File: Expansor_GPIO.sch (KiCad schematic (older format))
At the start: 6 parts

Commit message: version preliminar de la etapa de alimentacion
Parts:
- gave numbers to parts that had none: 6
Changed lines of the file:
@@
 LIBS:Sensores
 LIBS:Reles
+LIBS:Reguladores
+LIBS:Transistores
 LIBS:Wifi_PB-cache
 EELAYER 26 0
@@
 $Descr A4 11693 8268
 encoding utf-8
-Sheet 5 11
+Sheet 5 15
 Title ""
 Date "2017-01-15"
@@
 $EndDescr
 $Comp
-L MCP23017 U?
+L MCP23017 U6
 U 1 1 587AB386
 P 3300 2800
-F 0 "U?" H 3650 1800 50  0000 C CNN
+F 0 "U6" H 3650 1800 50  0000 C CNN
 F 1 "MCP23017" H 3350 2800 50  0000 C CNN
 F 2 "" H 3350 1850 50  0001 L CNN
@@
 $EndComp
 $Comp
-L CP1 C?
+L CP1 C14
 U 1 1 587AB690
 P 2450 1400
-F 0 "C?" H 2565 1446 50  0000 L CNN
+F 0 "C14" H 2565 1446 50  0000 L CNN
 F 1 "CP1" H 2565 1355 50  0000 L CNN
-F 2 "" H 2450 1400 50  0000 C CNN
+F 2 "" H 2450 1400 50  0001 C CNN
 F 3 "" H 2450 1400 50  0000 C CNN
 	1    2450 1400
@@
 $EndComp
 $Comp
-L C C?
+L C C16
 U 1 1 587AB6AE
 P 2900 1400
-F 0 "C?" H 3015 1446 50  0000 L CNN
+F 0 "C16" H 3015 1446 50  0000 L CNN
 F 1 "C" H 3015 1355 50  0000 L CNN
-F 2 "" H 2938 1250 50  0000 C CNN
+F 2 "" H 2938 1250 50  0001 C CNN
 F 3 "" H 2900 1400 50  0000 C CNN
 	1    2900 1400
@@
 $EndComp
 $Comp
-L GND #PWR044
+L GND #PWR39
 U 1 1 587AB8C8
 P 3300 3900
-F 0 "#PWR044" H 3300 3650 50  0001 C CNN
+F 0 "#PWR39" H 3300 3650 50  0001 C CNN
 F 1 "GND" H 3305 3727 50  0000 C CNN
 F 2 "" H 3300 3900 50  0000 C CNN
@@
 	3300 3900 3300 3800
 $Comp
-L GND #PWR045
+L GND #PWR35
 U 1 1 587AB8EE
 P 2700 3900
-F 0 "#PWR045" H 2700 3650 50  0001 C CNN
+F 0 "#PWR35" H 2700 3650 50  0001 C CNN
 F 1 "GND" H 2705 3727 50  0000 C CNN
 F 2 "" H 2700 3900 50  0000 C CNN
@@
 	2450 1050 2450 1250
 $Comp
-L GND #PWR046
+L GND #PWR32
 U 1 1 587ABE16
 P 2450 1600
-F 0 "#PWR046" H 2450 1350 50  0001 C CNN
+F 0 "#PWR32" H 2450 1350 50  0001 C CNN
 F 1 "GND" H 2455 1427 50  0000 C CNN
 F 2 "" H 2450 1600 50  0000 C CNN
@@
 Connection ~ 2900 1200
 $Comp
-L GND #PWR047
+L GND #PWR37
 U 1 1 587ABE80
 P 2900 1600
-F 0 "#PWR047" H 2900 1350 50  0001 C CNN
+F 0 "#PWR37" H 2900 1350 50  0001 C CNN
 F 1 "GND" H 2905 1427 50  0000 C CNN
 F 2 "" H 2900 1600 50  0000 C CNN
@@
 $EndComp
 $Comp
-L +5V #PWR048
+L +5V #PWR31
 U 1 1 587ABF96
 P 2450 1050
-F 0 "#PWR048" H 2450 900 50  0001 C CNN
+F 0 "#PWR31" H 2450 900 50  0001 C CNN
 F 1 "+5V" H 2465 1223 50  0000 C CNN
 F 2 "" H 2450 1050 50  0000 C CNN
@@
 	2350 3200 2800 3200
 $Comp
-L MCP23017 U?
+L MCP23017 U7
 U 1 1 587C555D
 P 3300 6250
-F 0 "U?" H 3650 5250 50  0000 C CNN
+F 0 "U7" H 3650 5250 50  0000 C CNN
 F 1 "MCP23017" H 3350 6250 50  0000 C CNN
 F 2 "" H 3350 5300 50  0001 L CNN
@@
 $EndComp
 $Comp
-L CP1 C?
+L CP1 C15
 U 1 1 587C5564
 P 2450 4850
-F 0 "C?" H 2565 4896 50  0000 L CNN
+F 0 "C15" H 2565 4896 50  0000 L CNN
 F 1 "CP1" H 2565 4805 50  0000 L CNN
-F 2 "" H 2450 4850 50  0000 C CNN
+F 2 "" H 2450 4850 50  0001 C CNN
 F 3 "" H 2450 4850 50  0000 C CNN
 	1    2450 4850
@@
 $EndComp
 $Comp
-L C C?
+L C C17
 U 1 1 587C556B
 P 2900 4850
-F 0 "C?" H 3015 4896 50  0000 L CNN
+F 0 "C17" H 3015 4896 50  0000 L CNN
 F 1 "C" H 3015 4805 50  0000 L CNN
-F 2 "" H 2938 4700 50  0000 C CNN
+F 2 "" H 2938 4700 50  0001 C CNN
 F 3 "" H 2900 4850 50  0000 C CNN
 	1    2900 4850
@@
 $EndComp
 $Comp
-L GND #PWR?
+L GND #PWR40
 U 1 1 587C5572
 P 3300 7350
-F 0 "#PWR?" H 3300 7100 50  0001 C CNN
+F 0 "#PWR40" H 3300 7100 50  0001 C CNN
 F 1 "GND" H 3305 7177 50  0000 C CNN
 F 2 "" H 3300 7350 50  0000 C CNN
@@
 	3300 7350 3300 7250
 $Comp
-L GND #PWR?
+L GND #PWR36
 U 1 1 587C5579
 P 2700 7350
-F 0 "#PWR?" H 2700 7100 50  0001 C CNN
+F 0 "#PWR36" H 2700 7100 50  0001 C CNN
 F 1 "GND" H 2705 7177 50  0000 C CNN
 F 2 "" H 2700 7350 50  0000 C CNN
@@
 	2450 4500 2450 4700
 $Comp
-L GND #PWR?
+L GND #PWR34
 U 1 1 587C55A2
 P 2450 5050
-F 0 "#PWR?" H 2450 4800 50  0001 C CNN
+F 0 "#PWR34" H 2450 4800 50  0001 C CNN
 F 1 "GND" H 2455 4877 50  0000 C CNN
 F 2 "" H 2450 5050 50  0000 C CNN
@@
 Connection ~ 2900 4650
 $Comp
-L GND #PWR?
+L GND #PWR38
 U 1 1 587C55AC
 P 2900 5050
-F 0 "#PWR?" H 2900 4800 50  0001 C CNN
+F 0 "#PWR38" H 2900 4800 50  0001 C CNN
 F 1 "GND" H 2905 4877 50  0000 C CNN
 F 2 "" H 2900 5050 50  0000 C CNN
@@
 $EndComp
 $Comp
-L +5V #PWR?
+L +5V #PWR33
 U 1 1 587C55B2
 P 2450 4500
-F 0 "#PWR?" H 2450 4350 50  0001 C CNN
+F 0 "#PWR33" H 2450 4350 50  0001 C CNN
 F 1 "+5V" H 2465 4673 50  0000 C CNN
 F 2 "" H 2450 4500 50  0000 C CNN

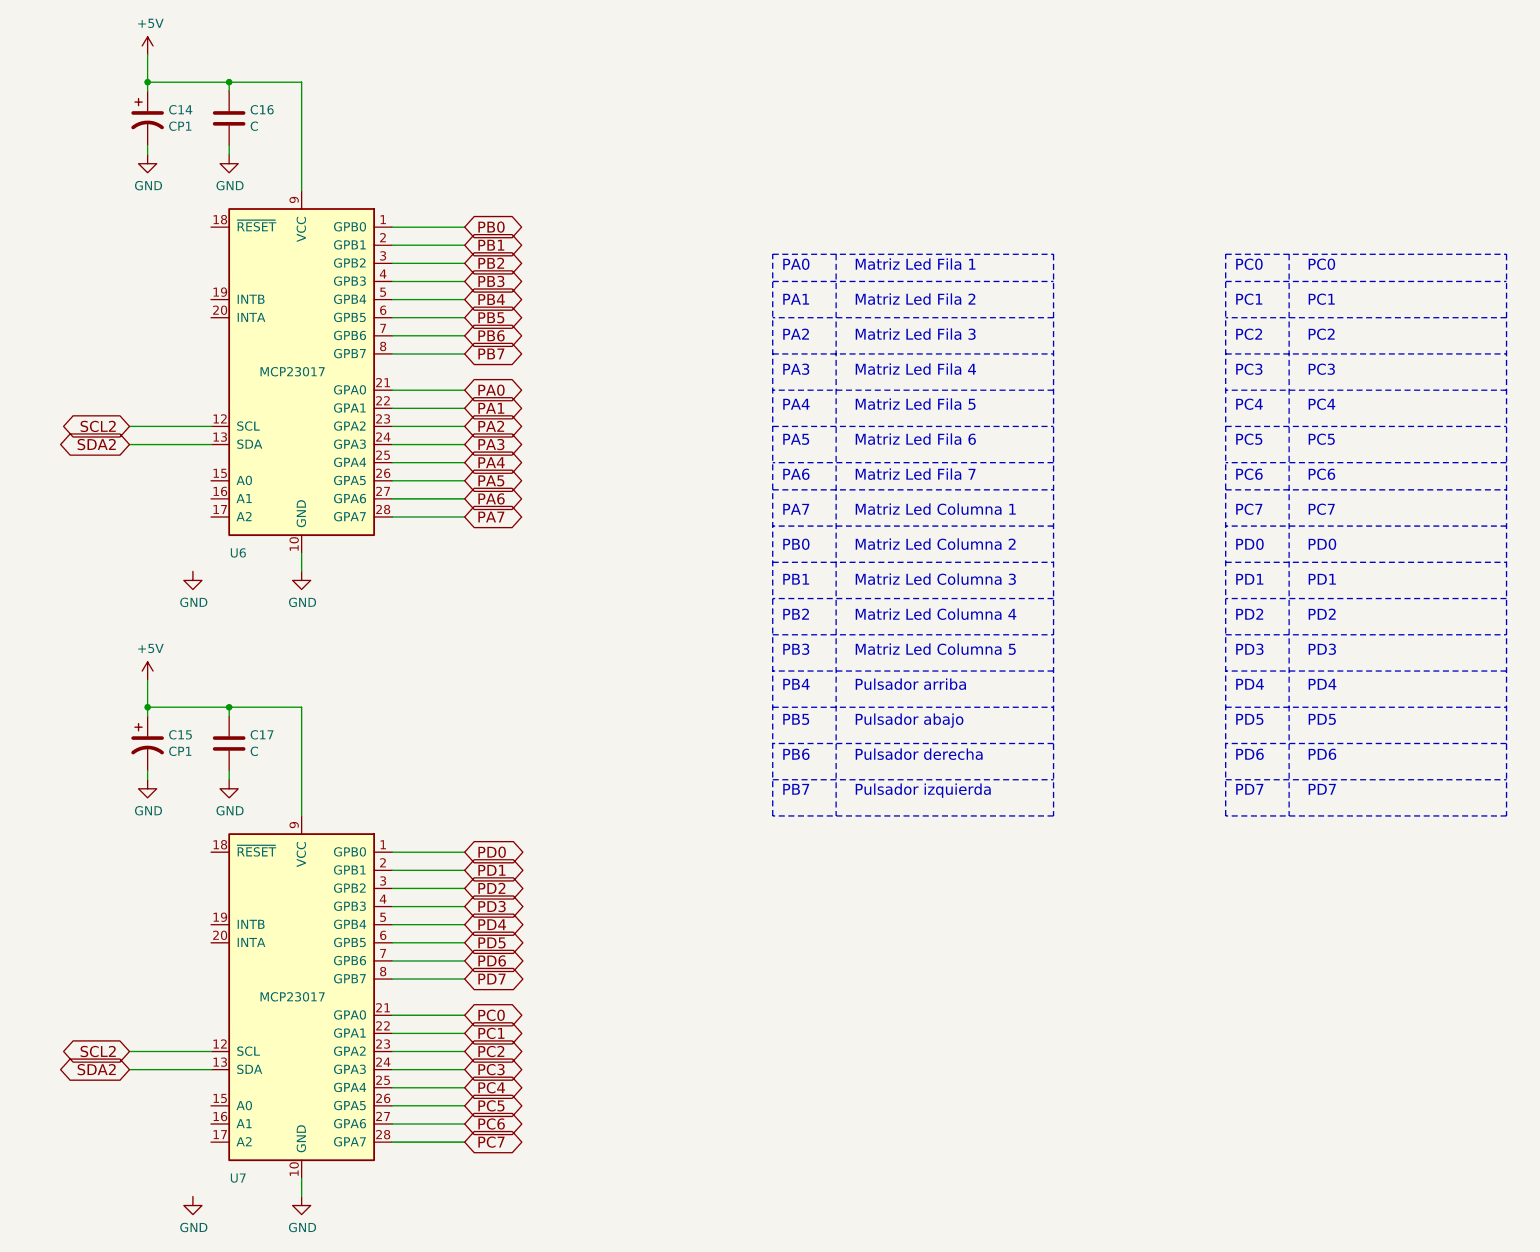
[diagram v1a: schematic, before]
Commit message: asignacion inicial de huellas
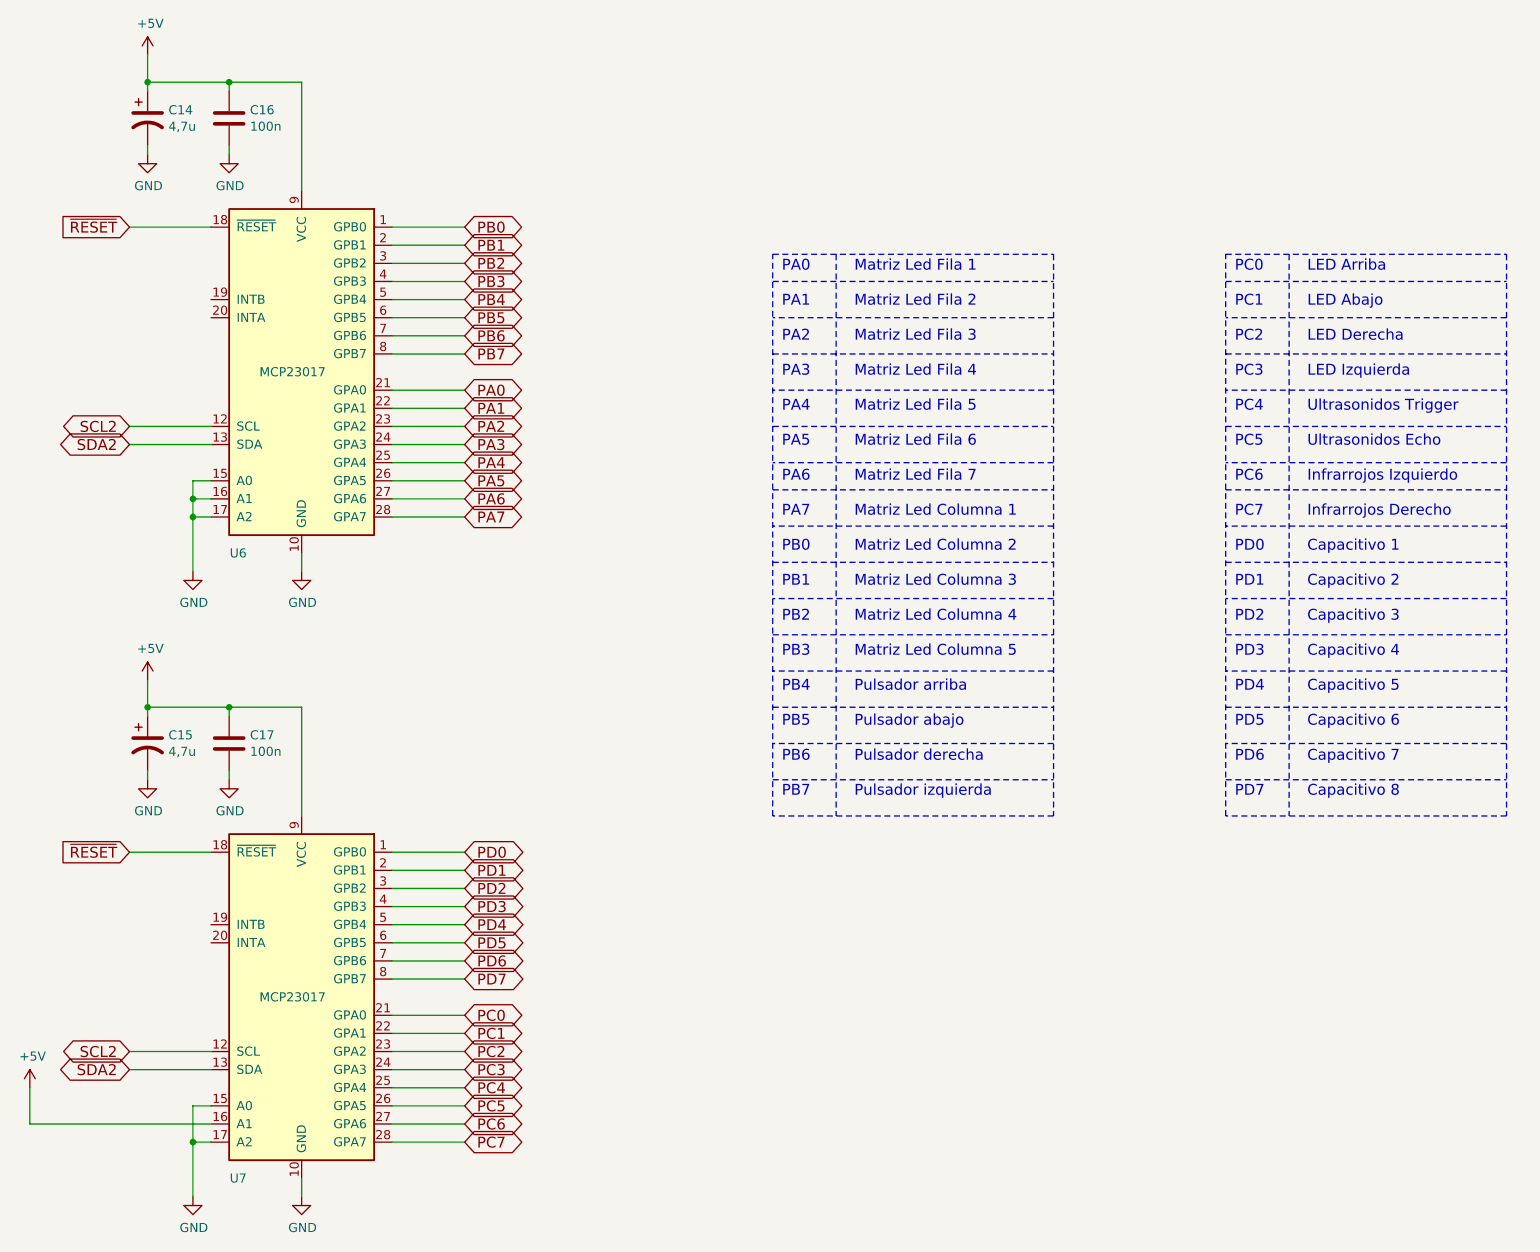
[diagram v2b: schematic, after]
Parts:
- C14, C15: value CP1 -> 4,7u; footprint (none) -> Capacitors_SMD:C_1206
- C16, C17: value C -> 100n; footprint (none) -> Capacitors_SMD:C_0805
- U6, U7: footprint (none) -> Housings_SSOP:SSOP-28_5.3x10.2mm_Pitch0.65mm
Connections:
- net +5V: now also U7.16 (A1)
- net GND: now also U6.15 (A0), U6.16 (A1), U6.17 (A2), U7.15 (A0), U7.17 (A2)
- net ~RESET: now reaches U6.18 (~RESET)
- net ~RESET: now also U7.18 (~RESET)
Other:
- note added: "LED Arriba\n\nLED Abajo\n\nLED Derecha\n\nLED Izquierda\n\nUltrasonidos Trigger\n\nUltrasonidos Echo\n\nInfrarrojos Izquierdo\n\nInfrarrojos Derecho\n\nCapacitivo 1\n\nCapacitivo 2\n\nCapacitivo 3\n\nCapacitivo 4\n\nCapacitivo 5\n\nCapacitivo 6\n\nCapacitivo 7\n\nCapacitivo 8"
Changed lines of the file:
@@
 F 0 "U6" H 3650 1800 50  0000 C CNN
 F 1 "MCP23017" H 3350 2800 50  0000 C CNN
-F 2 "" H 3350 1850 50  0001 L CNN
+F 2 "Housings_SSOP:SSOP-28_5.3x10.2mm_Pitch0.65mm" H 3350 1850 50  0001 L CNN
 F 3 "" H 3550 3800 50  0001 C CNN
 F 4 "MICROCHIP TECHNOLOGY" H 3300 2800 60  0001 C CNN "Fabricante"
@@
 P 2450 1400
 F 0 "C14" H 2565 1446 50  0000 L CNN
-F 1 "CP1" H 2565 1355 50  0000 L CNN
-F 2 "" H 2450 1400 50  0001 C CNN
+F 1 "4,7u" H 2565 1355 50  0000 L CNN
+F 2 "Capacitors_SMD:C_1206" H 2450 1400 50  0001 C CNN
 F 3 "" H 2450 1400 50  0000 C CNN
 	1    2450 1400
@@
 P 2900 1400
 F 0 "C16" H 3015 1446 50  0000 L CNN
-F 1 "C" H 3015 1355 50  0000 L CNN
-F 2 "" H 2938 1250 50  0001 C CNN
+F 1 "100n" H 3015 1355 50  0000 L CNN
+F 2 "Capacitors_SMD:C_0805" H 2938 1250 50  0001 C CNN
 F 3 "" H 2900 1400 50  0000 C CNN
 	1    2900 1400
@@
 $EndComp
 $Comp
-L GND #PWR39
+L GND #PWR044
 U 1 1 587AB8C8
 P 3300 3900
-F 0 "#PWR39" H 3300 3650 50  0001 C CNN
+F 0 "#PWR044" H 3300 3650 50  0001 C CNN
 F 1 "GND" H 3305 3727 50  0000 C CNN
 F 2 "" H 3300 3900 50  0000 C CNN
@@
 	3300 3900 3300 3800
 $Comp
-L GND #PWR35
+L GND #PWR045
 U 1 1 587AB8EE
 P 2700 3900
-F 0 "#PWR35" H 2700 3650 50  0001 C CNN
+F 0 "#PWR045" H 2700 3650 50  0001 C CNN
 F 1 "GND" H 2705 3727 50  0000 C CNN
 F 2 "" H 2700 3900 50  0000 C CNN
@@
 	2450 1050 2450 1250
 $Comp
-L GND #PWR32
+L GND #PWR046
 U 1 1 587ABE16
 P 2450 1600
-F 0 "#PWR32" H 2450 1350 50  0001 C CNN
+F 0 "#PWR046" H 2450 1350 50  0001 C CNN
 F 1 "GND" H 2455 1427 50  0000 C CNN
 F 2 "" H 2450 1600 50  0000 C CNN
@@
 Connection ~ 2900 1200
 $Comp
-L GND #PWR37
+L GND #PWR047
 U 1 1 587ABE80
 P 2900 1600
-F 0 "#PWR37" H 2900 1350 50  0001 C CNN
+F 0 "#PWR047" H 2900 1350 50  0001 C CNN
 F 1 "GND" H 2905 1427 50  0000 C CNN
 F 2 "" H 2900 1600 50  0000 C CNN
@@
 $EndComp
 $Comp
-L +5V #PWR31
+L +5V #PWR048
 U 1 1 587ABF96
 P 2450 1050
-F 0 "#PWR31" H 2450 900 50  0001 C CNN
+F 0 "#PWR048" H 2450 900 50  0001 C CNN
 F 1 "+5V" H 2465 1223 50  0000 C CNN
 F 2 "" H 2450 1050 50  0000 C CNN
@@
 F 0 "U7" H 3650 5250 50  0000 C CNN
 F 1 "MCP23017" H 3350 6250 50  0000 C CNN
-F 2 "" H 3350 5300 50  0001 L CNN
+F 2 "Housings_SSOP:SSOP-28_5.3x10.2mm_Pitch0.65mm" H 3350 5300 50  0001 L CNN
 F 3 "" H 3550 7250 50  0001 C CNN
 F 4 "MICROCHIP TECHNOLOGY" H 3300 6250 60  0001 C CNN "Fabricante"
@@
 P 2450 4850
 F 0 "C15" H 2565 4896 50  0000 L CNN
-F 1 "CP1" H 2565 4805 50  0000 L CNN
-F 2 "" H 2450 4850 50  0001 C CNN
+F 1 "4,7u" H 2565 4805 50  0000 L CNN
+F 2 "Capacitors_SMD:C_1206" H 2450 4850 50  0001 C CNN
 F 3 "" H 2450 4850 50  0000 C CNN
 	1    2450 4850
@@
 P 2900 4850
 F 0 "C17" H 3015 4896 50  0000 L CNN
-F 1 "C" H 3015 4805 50  0000 L CNN
-F 2 "" H 2938 4700 50  0001 C CNN
+F 1 "100n" H 3015 4805 50  0000 L CNN
+F 2 "Capacitors_SMD:C_0805" H 2938 4700 50  0001 C CNN
 F 3 "" H 2900 4850 50  0000 C CNN
 	1    2900 4850
@@
 $EndComp
 $Comp
-L GND #PWR40
+L GND #PWR049
 U 1 1 587C5572
 P 3300 7350
-F 0 "#PWR40" H 3300 7100 50  0001 C CNN
+F 0 "#PWR049" H 3300 7100 50  0001 C CNN
 F 1 "GND" H 3305 7177 50  0000 C CNN
 F 2 "" H 3300 7350 50  0000 C CNN
@@
 	3300 7350 3300 7250
 $Comp
-L GND #PWR36
+L GND #PWR050
 U 1 1 587C5579
 P 2700 7350
-F 0 "#PWR36" H 2700 7100 50  0001 C CNN
+F 0 "#PWR050" H 2700 7100 50  0001 C CNN
 F 1 "GND" H 2705 7177 50  0000 C CNN
 F 2 "" H 2700 7350 50  0000 C CNN
@@
 	2450 4500 2450 4700
 $Comp
-L GND #PWR34
+L GND #PWR051
 U 1 1 587C55A2
 P 2450 5050
-F 0 "#PWR34" H 2450 4800 50  0001 C CNN
+F 0 "#PWR051" H 2450 4800 50  0001 C CNN
 F 1 "GND" H 2455 4877 50  0000 C CNN
 F 2 "" H 2450 5050 50  0000 C CNN
@@
 Connection ~ 2900 4650
 $Comp
-L GND #PWR38
+L GND #PWR052
 U 1 1 587C55AC
 P 2900 5050
-F 0 "#PWR38" H 2900 4800 50  0001 C CNN
+F 0 "#PWR052" H 2900 4800 50  0001 C CNN
 F 1 "GND" H 2905 4877 50  0000 C CNN
 F 2 "" H 2900 5050 50  0000 C CNN
@@
 $EndComp
 $Comp
-L +5V #PWR33
+L +5V #PWR053
 U 1 1 587C55B2
 P 2450 4500
-F 0 "#PWR33" H 2450 4350 50  0001 C CNN
+F 0 "#PWR053" H 2450 4350 50  0001 C CNN
 F 1 "+5V" H 2465 4673 50  0000 C CNN
 F 2 "" H 2450 4500 50  0000 C CNN
@@
 PC0\n\nPC1\n\nPC2\n\nPC3\n\nPC4\n\nPC5\n\nPC6\n\nPC7\n\nPD0\n\nPD1\n\nPD2\n\nPD3\n\nPD4\n\nPD5\n\nPD6\n\nPD7
 Text Notes 8850 5150 0    60   ~ 0
-PC0\n\nPC1\n\nPC2\n\nPC3\n\nPC4\n\nPC5\n\nPC6\n\nPC7\n\nPD0\n\nPD1\n\nPD2\n\nPD3\n\nPD4\n\nPD5\n\nPD6\n\nPD7
+LED Arriba\n\nLED Abajo\n\nLED Derecha\n\nLED Izquierda\n\nUltrasonidos Trigger\n\nUltrasonidos Echo\n\nInfrarrojos Izquierdo\n\nInfrarrojos Derecho\n\nCapacitivo 1\n\nCapacitivo 2\n\nCapacitivo 3\n\nCapacitivo 4\n\nCapacitivo 5\n\nCapacitivo 6\n\nCapacitivo 7\n\nCapacitivo 8
 Wire Notes Line
 	8400 2300 9950 2300
@@
 Text GLabel 2350 6650 0    60   BiDi ~ 0
 SDA2
+Wire Wire Line
+	2350 2000 2800 2000
+Text GLabel 2350 2000 0    60   Input ~ 0
+~RESET
+Text GLabel 2350 5450 0    60   Input ~ 0
+~RESET
+Wire Wire Line
+	2350 5450 2800 5450
+Wire Wire Line
+	2700 3900 2700 3400
+Wire Wire Line
+	2700 3400 2800 3400
+Wire Wire Line
+	2700 3500 2800 3500
+Connection ~ 2700 3500
+Wire Wire Line
+	2800 3600 2700 3600
+Connection ~ 2700 3600
+Wire Wire Line
+	2800 6850 2700 6850
+Wire Wire Line
+	2700 6850 2700 7350
+Wire Wire Line
+	2700 7050 2800 7050
+Connection ~ 2700 7050
+Wire Wire Line
+	2800 6950 1800 6950
+Wire Wire Line
+	1800 6950 1800 6750
+$Comp
+L +5V #PWR054
+U 1 1 5891285D
+P 1800 6750
+F 0 "#PWR054" H 1800 6600 50  0001 C CNN
+F 1 "+5V" H 1815 6923 50  0000 C CNN
+F 2 "" H 1800 6750 50  0001 C CNN
+F 3 "" H 1800 6750 50  0001 C CNN
+	1    1800 6750
+	1    0    0    -1
+$EndComp
 $EndSCHEMATC
